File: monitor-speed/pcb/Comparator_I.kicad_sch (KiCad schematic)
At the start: 14 parts, among them K20 DIPxx-1Cxx-51x, Q2 BC848

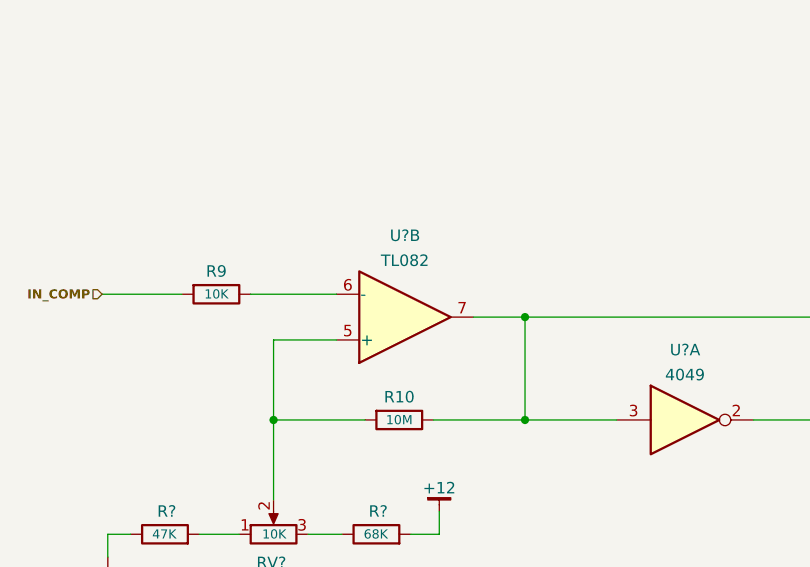
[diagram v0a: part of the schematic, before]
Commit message: Monitor-Speed: New Schematic
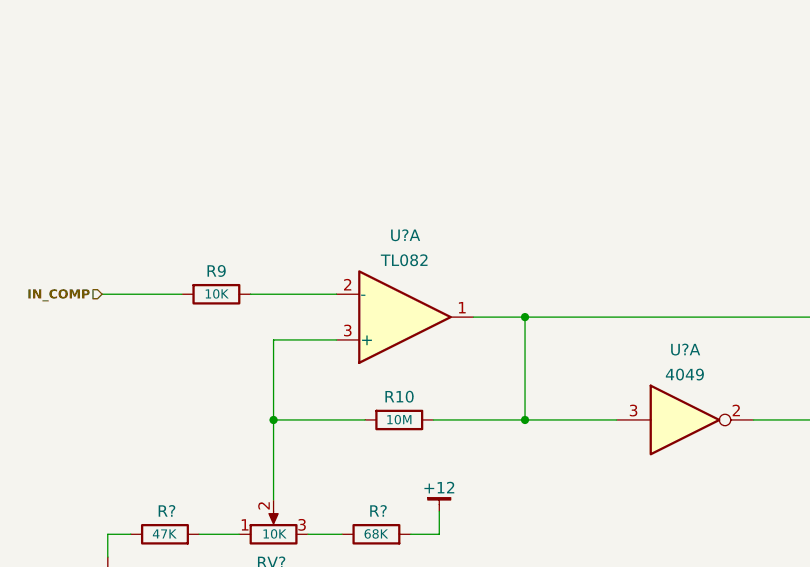
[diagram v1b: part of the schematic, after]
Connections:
- net OUT_COMP: now also U?.1; no longer U?.7
- net at R9.1: now also U?.2 (-); no longer U?.6 (-)
- net at R10.2, RV?.2: now also U?.3 (+); no longer U?.5 (+)
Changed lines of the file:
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@@
     (pin "1")
   )
-  (symbol (lib_id "Amplifier_Operational:TL082") (at 130.175 91.44 0) (mirror x) (unit 2)
+  (symbol (lib_id "Amplifier_Operational:TL082") (at 130.175 91.44 0) (mirror x) (unit 1)
     (in_bom yes) (on_board yes) (fields_autoplaced)
     (property "Reference" "U?" (id 0) (at 130.175 82.3935 0))
@@
       (effects (font (size 1.27 1.27)) hide)
     )
-    (pin "5")
-    (pin "6")
-    (pin "7")
+    (pin "1")
+    (pin "2")
+    (pin "3")
   )
   (symbol (lib_id "Device:R") (at 179.07 102.87 270) (unit 1)

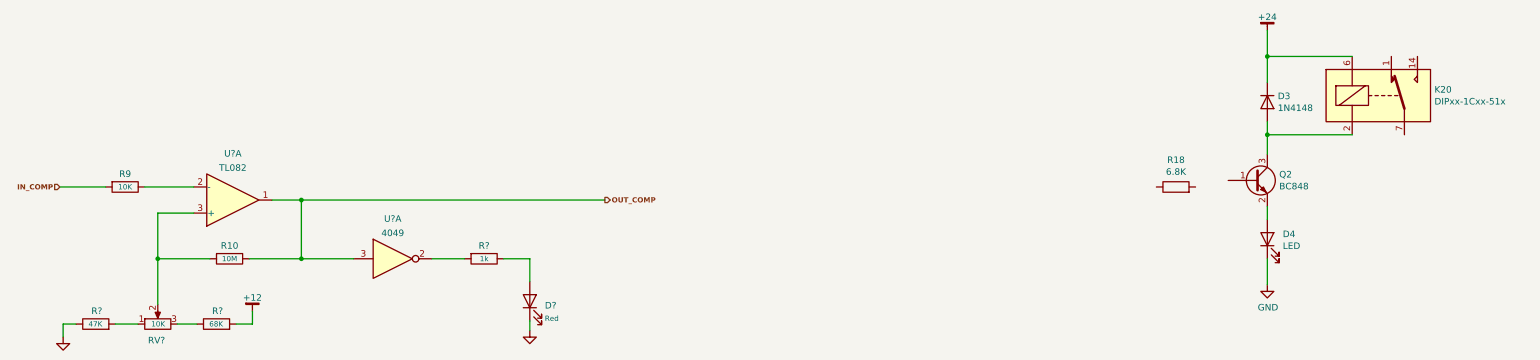
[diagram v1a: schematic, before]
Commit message: Monitor-Speed: Add Relay Circuit
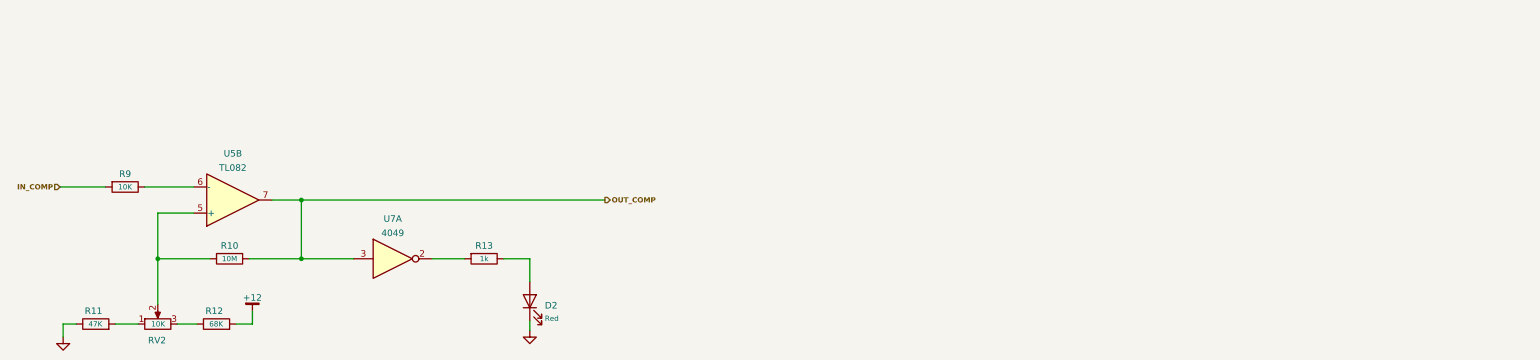
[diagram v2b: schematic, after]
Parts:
- removed D3: 1N4148, Diode_SMD:D_SOD-323, symbol Diode:1N4148
- removed D4: LED, LED_SMD:LED_1206_3216Metric, symbol Device:LED
- removed D?: Red, symbol Device:LED
- removed K20: DIPxx-1Cxx-51x, Relay_THT:Relay_StandexMeder_DIP_LowProfile, symbol Relay:DIPxx-1Cxx-51x
- removed Q2: BC848, Package_TO_SOT_SMD:SOT-23, symbol Transistor_BJT:BC848
- removed R18: 6.8K, Resistor_SMD:R_0603_1608Metric_Pad0.98x0.95mm_HandSolder, symbol Device:R
- removed R?: 47K, Resistor_SMD:R_0603_1608Metric_Pad0.98x0.95mm_HandSolder, symbol Device:R
- removed R?: 68K, Resistor_SMD:R_0603_1608Metric_Pad0.98x0.95mm_HandSolder, symbol Device:R
- removed R?: 1k, Resistor_SMD:R_0603_1608Metric_Pad0.98x0.95mm_HandSolder, symbol Device:R
- removed RV?: 10K, Potentiometer_SMD:Potentiometer_Vishay_TS53YL_Vertical, symbol Device:R_POT
- removed U?: 4049, symbol 4xxx:4049
- removed U?: TL082, symbol Amplifier_Operational:TL082
- added D2: Red, symbol Device:LED
- added R11: 47K, Resistor_SMD:R_0603_1608Metric_Pad0.98x0.95mm_HandSolder, symbol Device:R
- added R12: 68K, Resistor_SMD:R_0603_1608Metric_Pad0.98x0.95mm_HandSolder, symbol Device:R
- added R13: 1k, Resistor_SMD:R_0603_1608Metric_Pad0.98x0.95mm_HandSolder, symbol Device:R
- added RV2: 10K, Potentiometer_SMD:Potentiometer_Vishay_TS53YL_Vertical, symbol Device:R_POT
- added U5: TL082, symbol Amplifier_Operational:TL082
- added U7: 4049, symbol 4xxx:4049
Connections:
- net +12: now also R12.2
- net GND: now also D2.1 (K), R11.1
- net OUT_COMP: now also U5.7, U7.3
- net at R9.1: now also U5.6 (-)
- net at R10.2: now also RV2.2, U5.5 (+)
- new net: D2.2 (A), R13.1
- new net: R13.2, U7.2
- new net: R12.1, RV2.3
- new net: R11.2, RV2.1
